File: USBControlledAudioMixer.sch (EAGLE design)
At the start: 52 parts, among them IC1 TDA7448, IC2 TS912, IC3 MEGA8-AI, J2 AVR_SPI_PRG_6NS, Q1 16MHz, U1 LMR62014

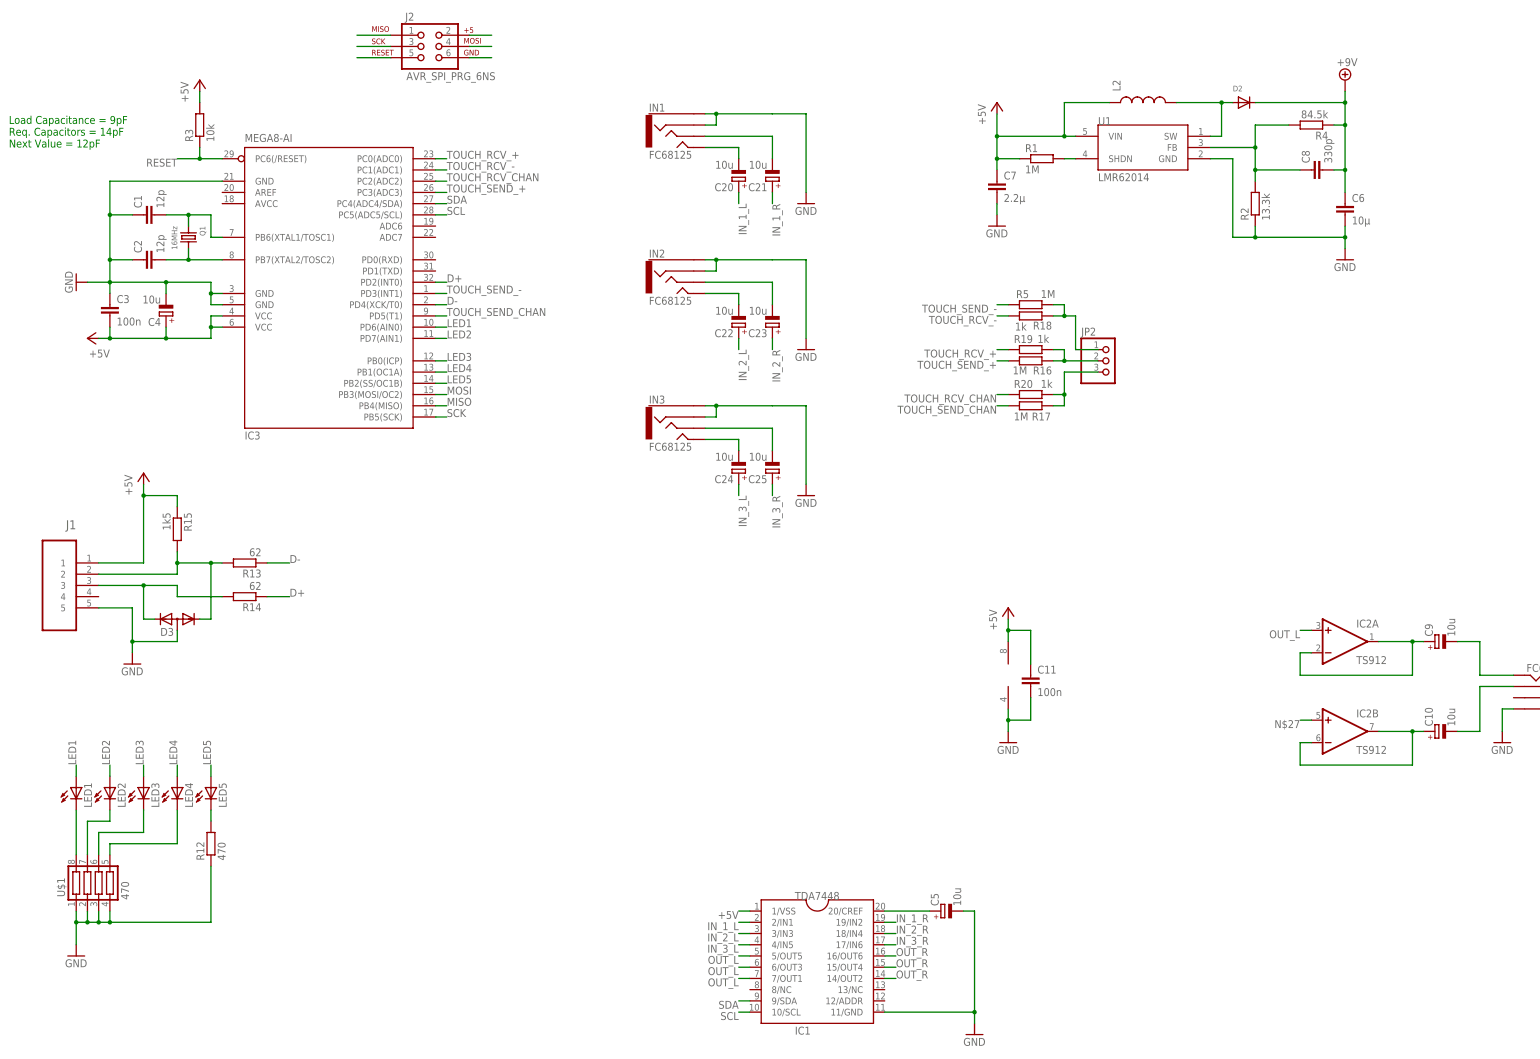
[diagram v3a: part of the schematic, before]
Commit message: Routing done, silkscreen adjustments missing
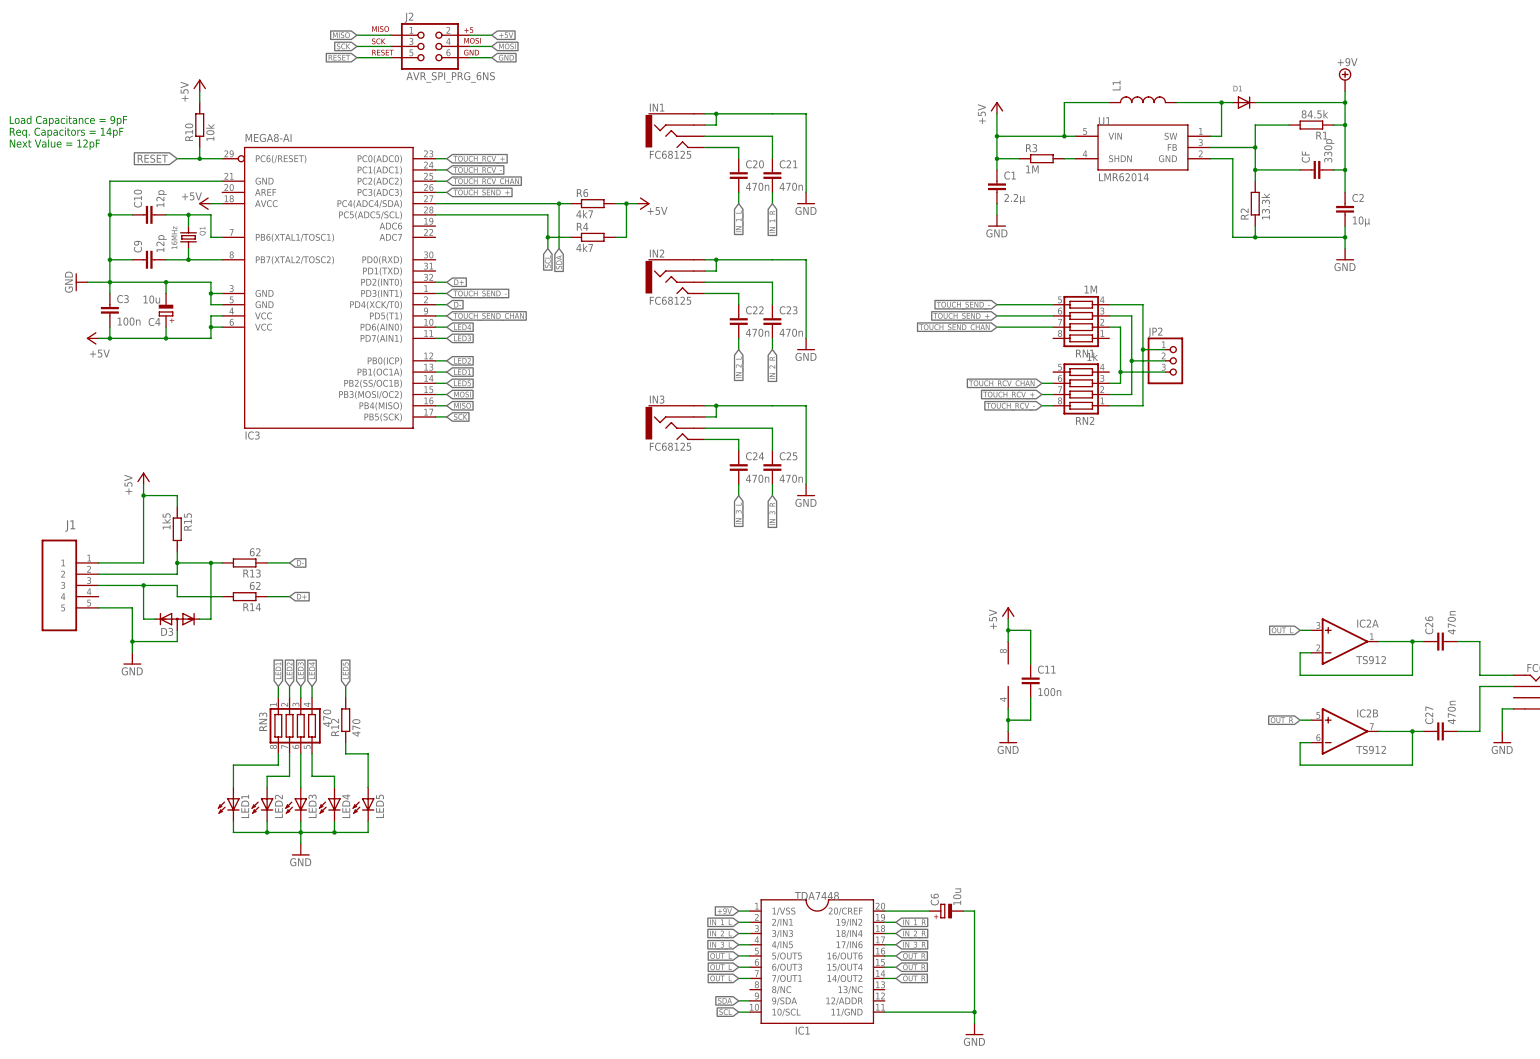
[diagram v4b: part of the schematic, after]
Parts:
- removed C5: 10u, rcl:CPOL-EUA/3216-18W
- removed C7: 2.2µ, rcl:C-EUC0603
- removed R16, R17, R5: 1M, rcl:R-EU_R0603
- removed R18, R19, R20: 1k, rcl:R-EU_R0603
- removed U$1: 470, Simplex-rlc:RES_ARR
- added C26, C27: 470n, rcl:C-EU025-050X050
- added R10: 10k, rcl:R-EU_R0603
- added R6: 4k7, rcl:R-EU_R0603
- added RN1: 1M, Simplex-rlc:RES_ARR
- added RN2: 1k, Simplex-rlc:RES_ARR
- added RN3: 470, Simplex-rlc:RES_ARR
- C1: value 12p -> 2.2µ; OC_DIGIKEY 1276-1254-1-ND -> 1276-1821-1-ND; PRICE_100 0.013 -> 0.039
- C10: value 10u -> 12p; device rcl:CPOL-EU153CLV-0405 -> rcl:C-EUC0603; OC_DIGIKEY 493-2173-1-ND -> 1276-1254-1-ND; PRICE_100 0.127 -> 0.013
- C2: value 12p -> 10µ; device rcl:C-EUC0603 -> rcl:C-EUC0805; OC_DIGIKEY (none) -> 490-10498-1-ND; OC_TME CL21C220JBANNNC -> (none); PRICE_100 (none) -> 0.067
- C20, C21, C22, C23, C24, C25: value 10u -> 470n; device rcl:CPOL-EU153CLV-0405 -> rcl:C-EU025-050X050; OC_DIGIKEY 493-2173-1-ND -> (none); OC_TME (none) -> MKS02-470N/63; PRICE_100 0.127 -> 0.19
- C6: value 10µ -> 10u; device rcl:C-EUC0805 -> rcl:CPOL-EUSMCA; OC_DIGIKEY 490-10498-1-ND -> (none); OC_TME (none) -> TAJA155K016R; PRICE_100 0.067 -> 0.059
- C9: value 10u -> 12p; device rcl:CPOL-EU153CLV-0405 -> rcl:C-EUC0603; OC_DIGIKEY 493-2173-1-ND -> (none); OC_TME (none) -> CL21C220JBANNNC; PRICE_100 0.127 -> (none)
- LED1, LED2, LED3, LED4, LED5: device led:LEDCHIPLED-0603-TTW -> SparkFun:LED0603
- R1: value 1M -> 84.5k; OC_DIGIKEY RHM1MCGCT-ND -> RHM84.5KCFCT-ND; PRICE_100 0.0043 -> 0.0048
- R3: value 10k -> 1M; OC_DIGIKEY (none) -> RHM1MCGCT-ND; OC_TME SMD0805-10K -> (none); PRICE_100 (none) -> 0.0043
- R4: value 84.5k -> 4k7; OC_DIGIKEY RHM84.5KCFCT-ND -> RHM4.7KCGCT-ND; PRICE_100 0.0048 -> 0.0043
- renumbered C8 to CF, D2 to D1, L2 to L1
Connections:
- net N$22 renamed SW
- removed net N$21: R1.2, U1.SHDN
- removed net N$25: CF.1, R2.2, R4.2, U1.FB
- removed net N$27: IC2B.+IN
- new net FB: CF.1, R1.2, R2.2, U1.FB
- new net N$100: C27.1, IC2B.-IN, IC2B.OUT
- new net SHDN: R3.2, U1.SHDN
- net +5V: now also C1.1, IC3.AVCC, R10.2, R3.1, R4.2, R6.2; no longer C7.1, IC1.1/VSS, R1.1, R3.2
- net +9V: now also C2.1, IC1.1/VSS, R1.1; no longer C6.1, R4.1
- net GND: now also C1.2, C10.1, C2.2, C6.-, C9.1, LED1.C, LED2.C, LED3.C, LED4.C, LED5.C; no longer C1.1, C2.1, C5.-, C6.2, C7.2, R12.1, U$1.1, U$1.2, U$1.3, U$1.4
- net IN_1_L: now also C20.2; no longer C20.+
- net IN_1_R: now also C21.2; no longer C21.+
- net IN_2_L: now also C22.2; no longer C22.+
- net IN_2_R: now also C23.2; no longer C23.+
- net IN_3_L: now also C24.2; no longer C24.+
- net IN_3_R: now also C25.2; no longer C25.+
- net LED1: now also IC3.PB1(OC1A), RN3.1; no longer IC3.PD6(AIN0), LED1.A
- net LED2: now also IC3.PB0(ICP), RN3.2; no longer IC3.PD7(AIN1), LED2.A
- net LED3: now also IC3.PD7(AIN1), RN3.3; no longer IC3.PB0(ICP), LED3.A
- net LED4: now also IC3.PD6(AIN0), RN3.4; no longer IC3.PB1(OC1A), LED4.A
- net LED5: now also R12.2; no longer LED5.A
- net N$1: now also C6.+; no longer C5.+
- net N$10: now also C24.1; no longer C24.-
- net N$12: now also C25.1; no longer C25.-
- net N$14: now also C22.1; no longer C22.-
- net N$15: now also C23.1; no longer C23.-
- net N$16: now also C20.1; no longer C20.-
- net N$17: now also C21.1; no longer C21.-
- net N$18: now also RN1.4, RN2.1; no longer R18.2, R5.2
- net N$19: now also RN1.3, RN2.2; no longer R16.2, R19.2
- net N$2: now also C9.2; no longer C2.2
- net N$20: now also RN1.2, RN2.3; no longer R17.2, R20.2
- net N$23: now also C26.2; no longer C9.-
- net N$24: now also C26.1; no longer C9.+
- net N$26: now also C27.2; no longer C10.-
- net N$3: now also C10.2; no longer C1.2
- net N$5: now also LED1.A, RN3.8; no longer LED1.C, U$1.8
- net N$6: now also LED2.A, RN3.7; no longer LED2.C, U$1.7
- net N$7: now also LED3.A, RN3.6; no longer LED3.C, U$1.6
- net N$8: now also LED4.A, RN3.5; no longer LED4.C, U$1.5
- net N$9: now also LED5.A, R12.1; no longer LED5.C, R12.2
- net OUT_R: now also IC2B.+IN; no longer C10.+, IC2B.-IN, IC2B.OUT
- net RESET: now also R10.1; no longer R3.1
- net SCL: now also R4.1
- net SDA: now also R6.1
- net TOUCH_RCV_+: now also RN2.7; no longer R19.1
- net TOUCH_RCV_-: now also RN2.8; no longer R18.1
- net TOUCH_RCV_CHAN: now also RN2.6; no longer R20.1
- net TOUCH_SEND_+: now also RN1.6; no longer R16.1
- net TOUCH_SEND_-: now also RN1.5; no longer R5.1
- net TOUCH_SEND_CHAN: now also RN1.7; no longer R17.1
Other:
- moved on the sheet: C1, C2, JP2, LED1, LED2, LED3, LED4, LED5, R1, R12, R3, R4

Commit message: Refactored whole board because due to case layout constraint, the regular through-hole film capacitors couldn't be used anymore. We're now using 1206 SMD film capacitors.
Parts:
- C20, C21, C22, C23, C24, C25, C26, C27: device rcl:C-EU025-050X050 -> rcl:C-EUC1206
- JP2: device pinhead:PINHD-1X3/90 -> TinyMix3:PINHD-1X3
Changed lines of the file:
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@@
 <?xml version="1.0" encoding="utf-8"?>
 <!DOCTYPE eagle SYSTEM "eagle.dtd">
-<eagle version="6.5.0">
+<eagle version="6.6.0">
 <drawing>
 <settings>
@@
 <attribute name="PRICE_100" value="0.0048"/>
 </part>
-<part name="JP2" library="pinhead" deviceset="PINHD-1X3" device="/90"/>
+<part name="JP2" library="TinyMix3" deviceset="PINHD-1X3" device=""/>
 <part name="J1" library="Molex-47346-0001" deviceset="47346-0001" device=""/>
 <part name="GND10" library="supply1" deviceset="GND" device=""/>
@@
 <attribute name="PRICE_100" value="0.008"/>
 </part>
-<part name="C24" library="rcl" deviceset="C-EU" device="025-050X050" value="470n">
-<attribute name="OC_TME" value="MKS02-470N/63"/>
-<attribute name="PRICE_100" value="0.19"/>
-</part>
-<part name="C25" library="rcl" deviceset="C-EU" device="025-050X050" value="470n">
-<attribute name="OC_TME" value="MKS02-470N/63"/>
-<attribute name="PRICE_100" value="0.19"/>
-</part>
-<part name="C22" library="rcl" deviceset="C-EU" device="025-050X050" value="470n">
-<attribute name="OC_TME" value="MKS02-470N/63"/>
-<attribute name="PRICE_100" value="0.19"/>
-</part>
-<part name="C23" library="rcl" deviceset="C-EU" device="025-050X050" value="470n">
-<attribute name="OC_TME" value="MKS02-470N/63"/>
-<attribute name="PRICE_100" value="0.19"/>
-</part>
-<part name="C20" library="rcl" deviceset="C-EU" device="025-050X050" value="470n">
-<attribute name="OC_TME" value="MKS02-470N/63"/>
-<attribute name="PRICE_100" value="0.19"/>
-</part>
-<part name="C21" library="rcl" deviceset="C-EU" device="025-050X050" value="470n">
-<attribute name="OC_TME" value="MKS02-470N/63"/>
-<attribute name="PRICE_100" value="0.19"/>
-</part>
-<part name="C26" library="rcl" deviceset="C-EU" device="025-050X050" value="470n">
-<attribute name="OC_TME" value="MKS02-470N/63"/>
-<attribute name="PRICE_100" value="0.19"/>
-</part>
-<part name="C27" library="rcl" deviceset="C-EU" device="025-050X050" value="470n">
-<attribute name="OC_TME" value="MKS02-470N/63"/>
-<attribute name="PRICE_100" value="0.19"/>
+<part name="C24" library="rcl" deviceset="C-EU" device="C1206" value="470n">
+<attribute name="OC_TME" value="MKS02-470N/63"/>
+<attribute name="PRICE_100" value="0.19"/>
+</part>
+<part name="C25" library="rcl" deviceset="C-EU" device="C1206" value="470n">
+<attribute name="OC_TME" value="MKS02-470N/63"/>
+<attribute name="PRICE_100" value="0.19"/>
+</part>
+<part name="C22" library="rcl" deviceset="C-EU" device="C1206" value="470n">
+<attribute name="OC_TME" value="MKS02-470N/63"/>
+<attribute name="PRICE_100" value="0.19"/>
+</part>
+<part name="C23" library="rcl" deviceset="C-EU" device="C1206" value="470n">
+<attribute name="OC_TME" value="MKS02-470N/63"/>
+<attribute name="PRICE_100" value="0.19"/>
+</part>
+<part name="C20" library="rcl" deviceset="C-EU" device="C1206" value="470n">
+<attribute name="OC_TME" value="MKS02-470N/63"/>
+<attribute name="PRICE_100" value="0.19"/>
+</part>
+<part name="C21" library="rcl" deviceset="C-EU" device="C1206" value="470n">
+<attribute name="OC_TME" value="MKS02-470N/63"/>
+<attribute name="PRICE_100" value="0.19"/>
+</part>
+<part name="C26" library="rcl" deviceset="C-EU" device="C1206" value="470n">
+<attribute name="OC_TME" value="MKS02-470N/63"/>
+<attribute name="PRICE_100" value="0.19"/>
+</part>
+<part name="C27" library="rcl" deviceset="C-EU" device="C1206" value="470n">
+<attribute name="OC_TME" value="MKS02-470N/63"/>
+<attribute name="PRICE_100" value="0.19"/>
